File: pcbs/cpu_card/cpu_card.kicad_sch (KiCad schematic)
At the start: 12 parts, among them J1 Conn1, J2 osc_header, U1 74LS161, Y1 ECS-2100AX-200

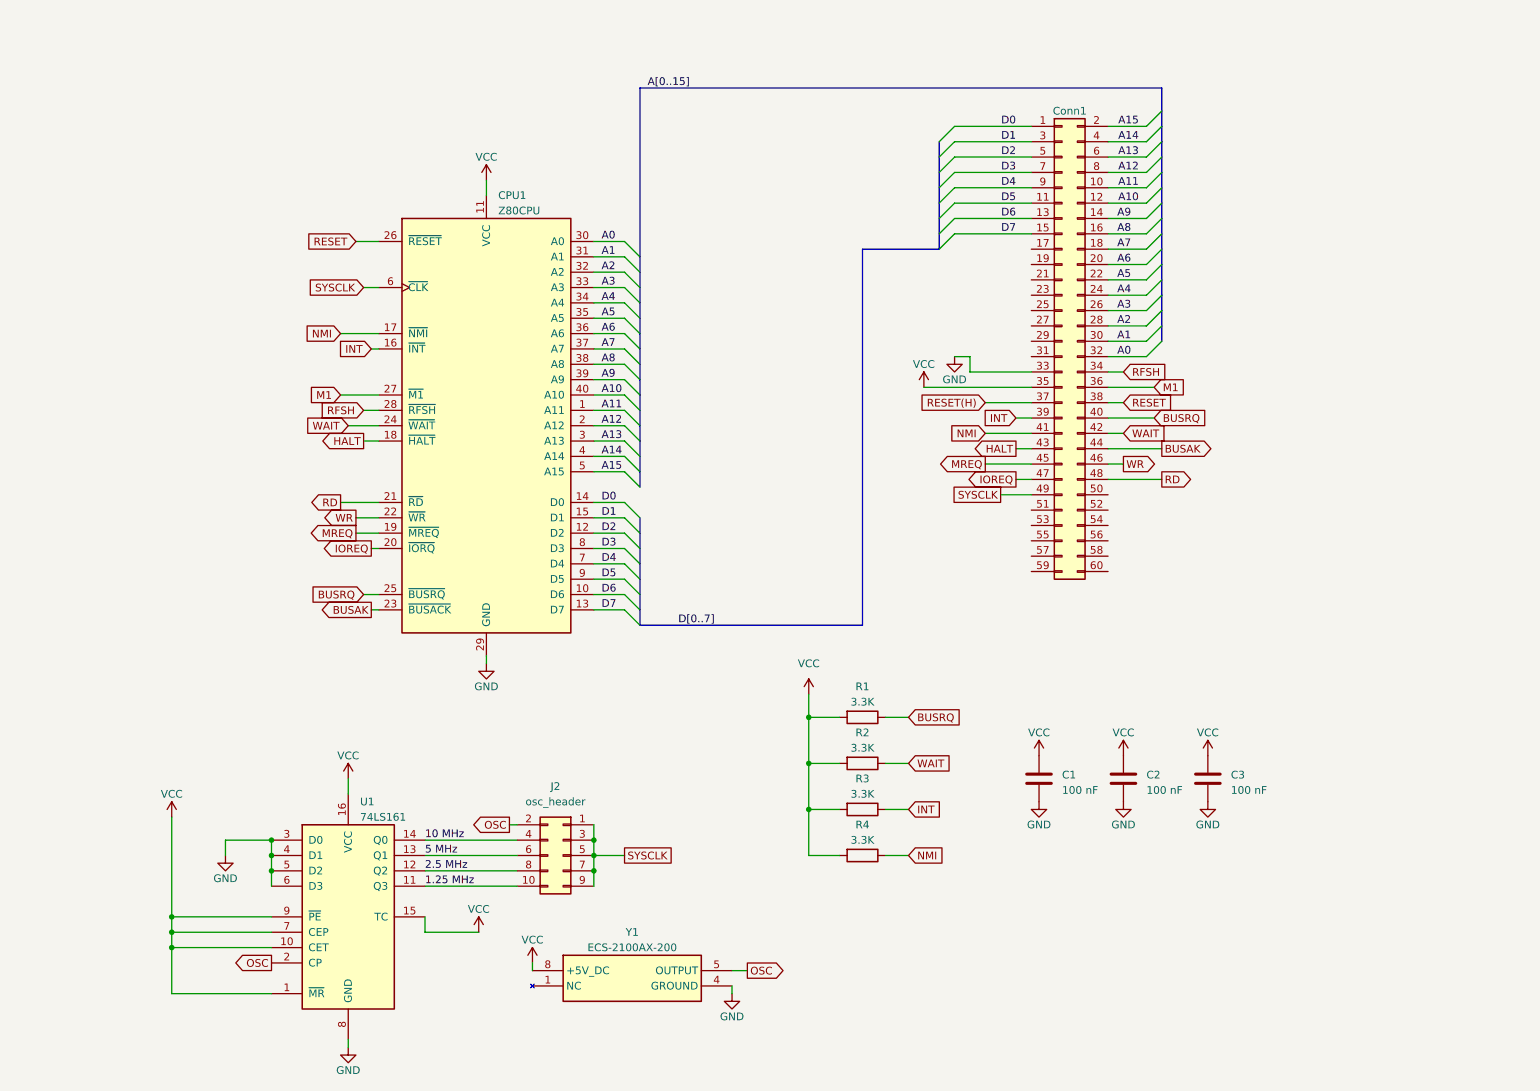
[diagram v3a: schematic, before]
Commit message: Mostly finished with cpu_card, added early prototypes of backplane and protoboard cards. Also added the libraries used for this project
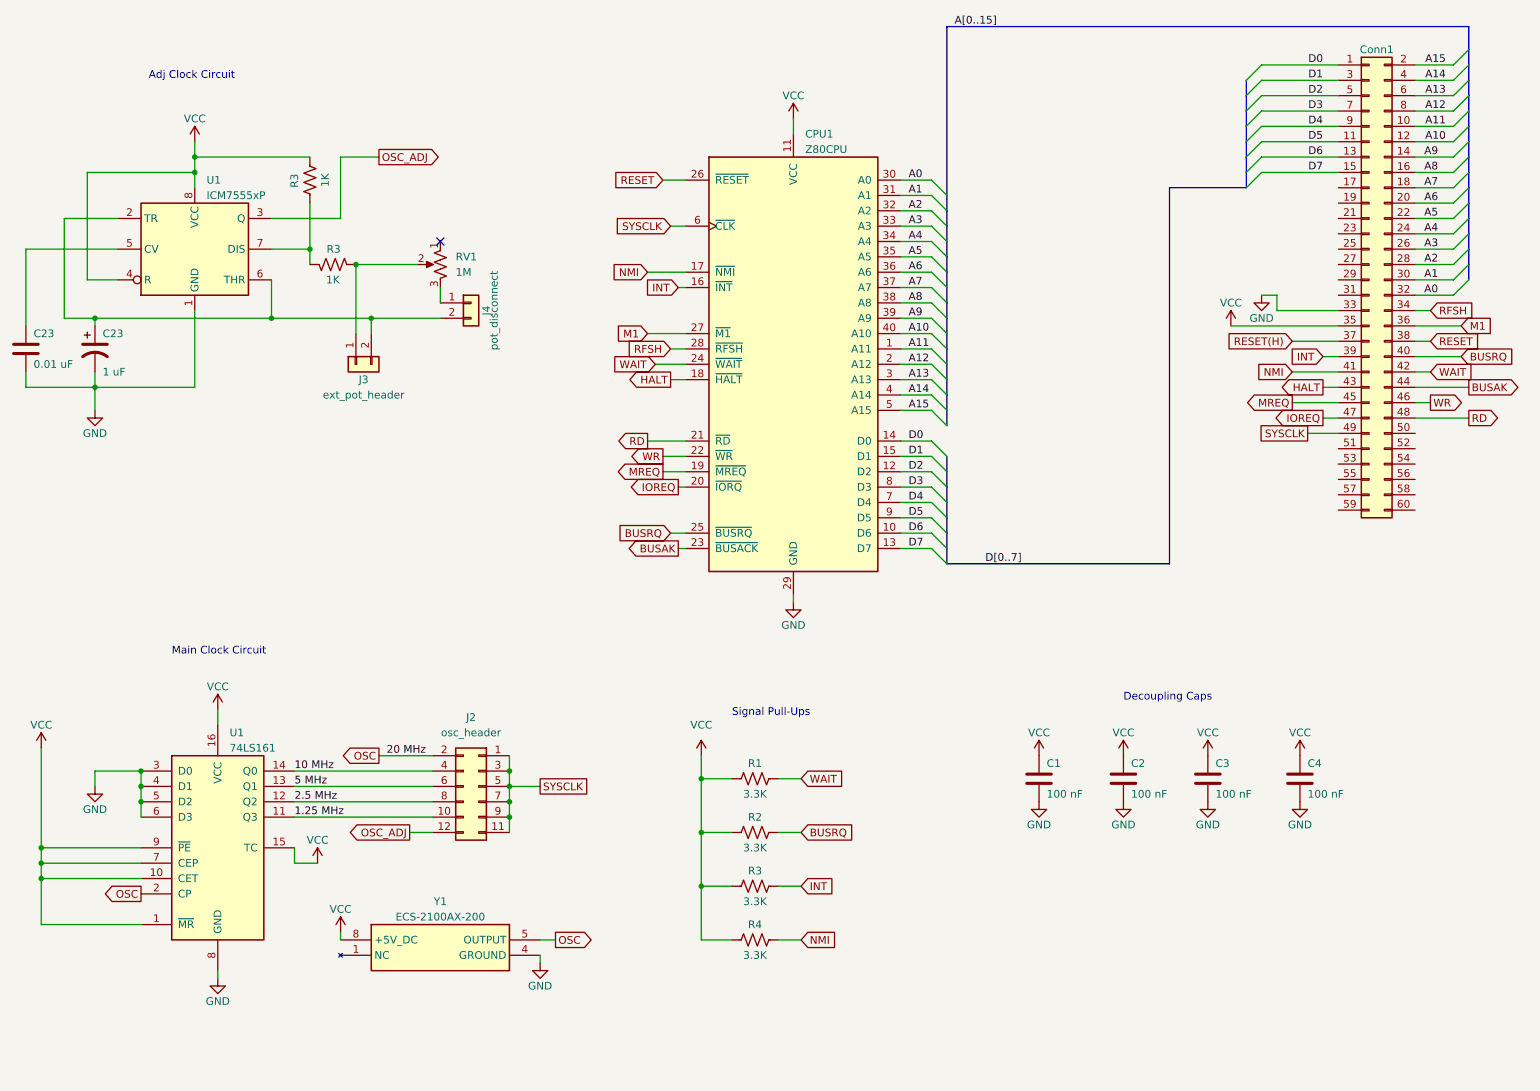
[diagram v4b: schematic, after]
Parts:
- added C23: 0.01 uF, Z80 Parts:C_Disc_D3.0mm_W1.6mm_P2.54mm, symbol Device:C
- added C23: 1 uF, Capacitor_THT:C_Radial_D5.0mm_H11.0mm_P2.00mm, symbol Device:C_Polarized_US
- added C4: 100 nF, Z80 Parts:C_Disc_D3.0mm_W1.6mm_P2.54mm, symbol Device:C
- added J3: ext_pot_header, Connector_PinHeader_2.54mm:PinHeader_1x02_P2.54mm_Vertical, symbol Connector_Generic:Conn_01x02
- added J4: pot_disconnect, Connector_PinHeader_2.54mm:PinHeader_1x02_P2.54mm_Vertical, symbol Connector_Generic:Conn_01x02
- added R3 (x2): 1K, Resistor_THT:R_Axial_DIN0204_L3.6mm_D1.6mm_P5.08mm_Horizontal, symbol Device:R_US
- added RV1: 1M, Potentiometer_THT:Potentiometer_Alpha_RD901F-40-00D_Single_Vertical, symbol Device:R_Potentiometer_US
- added U1: ICM7555xP, Package_DIP:DIP-8_W7.62mm, symbol Timer:ICM7555xP
- C1, C2, C3: footprint Capacitor_THT:C_Disc_D3.0mm_W1.6mm_P2.50mm -> Z80 Parts:C_Disc_D3.0mm_W1.6mm_P2.54mm
- J2: footprint Connector_PinHeader_2.54mm:PinHeader_2x05_P2.54mm_Vertical -> Connector_PinHeader_2.54mm:PinHeader_2x06_P2.54mm_Vertical; symbol Connector_Generic:Conn_02x05_Odd_Even -> Connector_Generic:Conn_02x06_Odd_Even
- R1, R2, R3, R4: symbol Device:R -> Device:R_US
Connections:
- net BUSRQ: now also R2.1; no longer R1.1
- net GND: now also C23.2, C23.2, C4.2, U1.1 (GND)
- net SYSCLK: now also J2.11 (Pin_11)
- net VCC: now also C4.1, R3.1, U1.4 (R), U1.8 (VCC)
- net WAIT: now also R1.1; no longer R2.1
- new net: C23.1, U1.5 (CV)
- new net: R3.1, R3.2, U1.7 (DIS)
- new net: J3.1 (Pin_1), R3.2, RV1.2
- new net: C23.1, J3.2 (Pin_2), J4.2 (Pin_2), U1.2 (TR), U1.6 (THR)
- new net: J4.1 (Pin_1), RV1.3
- new net OSC_ADJ: J2.12 (Pin_12), U1.3 (Q)
- no-connect marks 0 -> 1
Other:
- note added: "Adj Clock Circuit"
- note added: "Decoupling Caps"
- note added: "Main Clock Circuit"
- note added: "Signal Pull-Ups"
- moved on the sheet: CPU1, U1, Y1
